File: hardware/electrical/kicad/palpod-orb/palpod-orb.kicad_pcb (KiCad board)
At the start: 6 copper layers, 105 x 40 mm, 0 parts

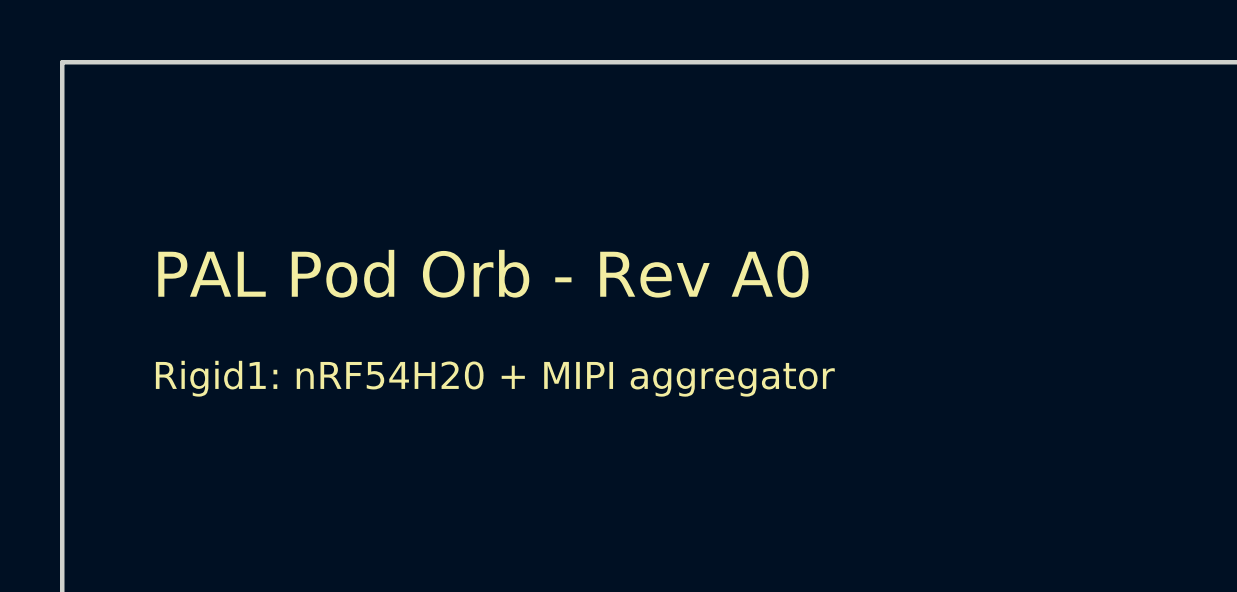
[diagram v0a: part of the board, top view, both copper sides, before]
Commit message: brand: sweep KiCad silkscreen + title metadata + Hey Pod wake word to Hearth
Follow-up to 3184563 rebrand sweep. Verifier caught KiCad title/company/
silkscreen "PAL Pod" strings that would be etched on physical PCBs if
fabricated — critical exposure.

Changes:
- .kicad_sch / .kicad_pcb / .kicad_pro title + company fields → Hearth /
  Hearth Home, Inc.
- gr_text silkscreen on F.SilkS layer → Hearth Orb - Rev A0 (physical)
- fp-lib-table + sym-lib-table description strings
- Wake word Hey Pod → Hey Hearth across all user-facing .md + .html

Not changed (still internal codenames per rebrand rules):
- Filenames (palpod-orb.kicad_sch etc.)
- Directory names (palpod-orb/, pal-web/, pal-voice/, pal-face/)
- Code identifiers (palpod_csrf, palpod_session, palpod_agent_token)
- Docker service names
- Wake-word ONNX model filename (hey_pod.onnx internally)
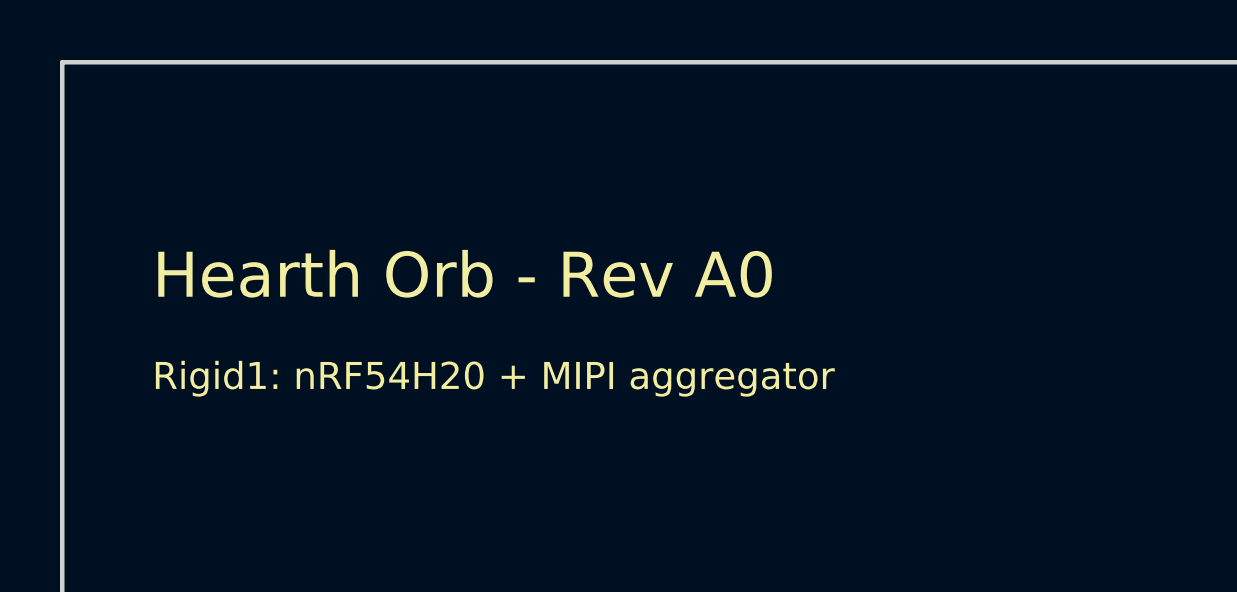
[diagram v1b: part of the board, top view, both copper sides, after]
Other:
- board text added: "Hearth Orb - Rev A0"
- board text removed: "PAL Pod Orb - Rev A0"
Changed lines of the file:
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@@
   (paper "A2")
   (title_block
-    (title "PAL Pod Orb - PCB (Flex-Rigid 6-Layer)")
+    (title "Hearth Orb - PCB (Flex-Rigid 6-Layer)")
     (date "2026-08-03")
     (rev "A0")
-    (company "PAL Pod")
+    (company "Hearth Home, Inc.")
     (comment 1 "6-layer flex-rigid: F.Cu / GND / PWR_3V3 / PWR_5V / GND / B.Cu")
     (comment 2 "Rigid: 1oz Cu on FR4. Flex: 0.5oz Cu on polyimide. ENIG.")
@@
   (gr_line (start 20 -7.5) (end 20 7.5) (stroke (width 0.15) (type solid)) (layer "Dwgs.User"))
   (gr_line (start 55 -7.5) (end 55 7.5) (stroke (width 0.15) (type solid)) (layer "Dwgs.User"))
-  (gr_text "PAL Pod Orb - Rev A0" (at -17 -12 0) (layer "F.SilkS") (effects (font (size 1.5 1.5) (thickness 0.2)) (justify left bottom)))
+  (gr_text "Hearth Orb - Rev A0" (at -17 -12 0) (layer "F.SilkS") (effects (font (size 1.5 1.5) (thickness 0.2)) (justify left bottom)))
   (gr_text "Rigid1: nRF54H20 + MIPI aggregator" (at -17 -9 0) (layer "F.SilkS") (effects (font (size 0.9 0.9) (thickness 0.12)) (justify left bottom)))
   (gr_text "Rigid2: SSD1963" (at 58 -6 0) (layer "F.SilkS") (effects (font (size 0.9 0.9) (thickness 0.12)) (justify left bottom)))
